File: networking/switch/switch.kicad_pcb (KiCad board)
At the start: 4 copper layers, 64.8 x 62.8 mm, 86 parts, among them J1 LDO IN, J3 3.3V IN, J4 PHY 5, J5 PHY 4, J6 PHY 3, J7 PHY 2, J8 PHY 1, SW1 AFT, SW2 F_PWR_OFF, T1 QT24A23-ALT, T2 QT24A23, U1 LM1117MP-3.3, U2 24LC01, U3 IP175G, U4 BT16A07, Y1 25MHz

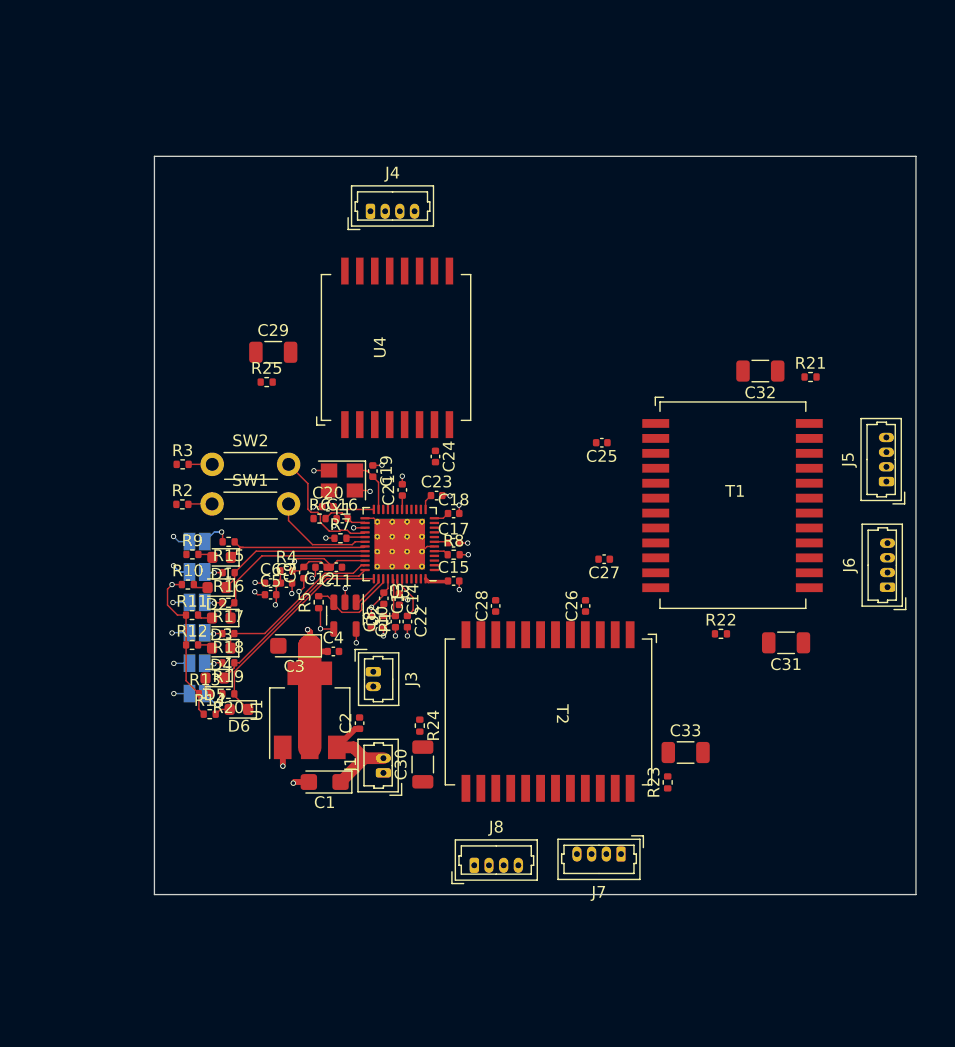
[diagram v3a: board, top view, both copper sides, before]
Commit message: Feat[switch]: Minor rerouting
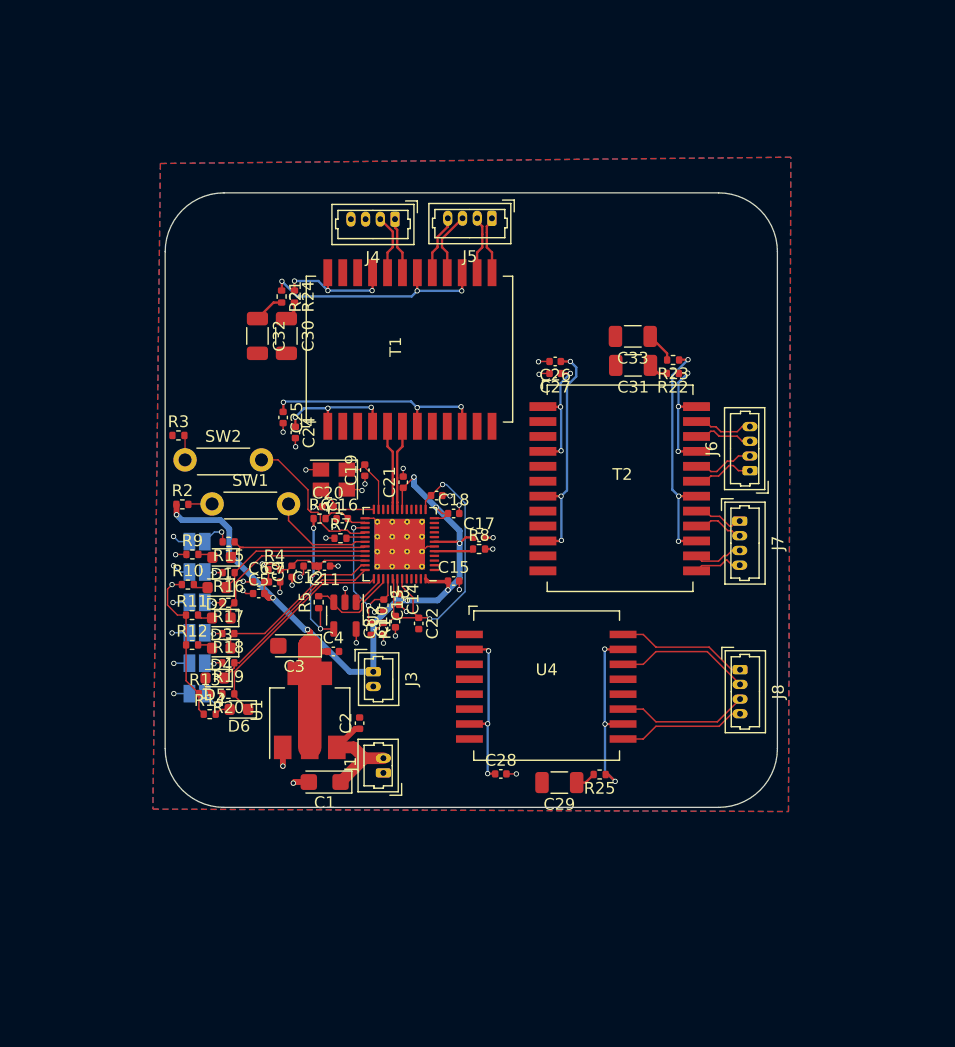
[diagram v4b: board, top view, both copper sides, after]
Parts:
- moved R21 45.5 mm to (114.9, 80.4), turned to -90 degrees
- moved C29 44.0 mm to (138.6, 121.7), turned to 180 degrees
- moved R25 43.8 mm to (142.0, 121.1), turned to 180 degrees
- moved C32 42.9 mm to (112.9, 83.8), turned to -90 degrees
- moved J5 40.3 mm to (132.8, 73.7), turned to 180 degrees
- moved C30 38.2 mm to (115.3, 83.8), turned to -90 degrees
- moved R24 38.0 mm to (116.0, 80.4)
- moved R23 35.9 mm to (148.2, 85.8), turned to 180 degrees
- moved C33 35.7 mm to (144.8, 83.8), turned to 180 degrees
- moved U4 31.4 mm to (137.4, 113.5), turned to 0 degrees
- moved T1 30.5 mm to (125.8, 84.9), turned to 90 degrees
- moved J7 30.1 mm to (153.9, 99.5), turned to -90 degrees
- moved J8 28.1 mm to (153.9, 112.1), turned to -90 degrees
- moved C25 27.2 mm to (115.1, 90.7), turned to -90 degrees
- moved C31 26.9 mm to (144.8, 86.3)
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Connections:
- C30 pad 1: /Magnetics/REF0 -> /Magnetics/REF4
- J8 pad 1: /Magnetics/RX0+ -> /Magnetics/TX0+
- J8 pad 2: /Magnetics/RX0- -> /Magnetics/TX0-
- J8 pad 3: /Magnetics/TX0+ -> /Magnetics/RX0+
- J8 pad 4: /Magnetics/TX0- -> /Magnetics/RX0-
- R24 pad 2: /Magnetics/REF0 -> /Magnetics/REF4
- R25 pad 1: /Magnetics/REF4 -> /Magnetics/REF0
- T1 pad 1: /Magnetics/CT3 -> /Magnetics/CT4
- T1 pad 10: /Magnetics/CT2 -> /Magnetics/CT3
- T1 pad 11: /IP175G/RXIM2 -> /IP175G/RXIM3
- T1 pad 12: /IP175G/RXIP2 -> /IP175G/RXIP3
- T1 pad 13: /Magnetics/RX2+ -> /Magnetics/RX3+
- T1 pad 14: /Magnetics/RX2- -> /Magnetics/RX3-
- T1 pad 15: Net-(R22-Pad1) -> Net-(R21-Pad1)
- T1 pad 16: /Magnetics/TX2+ -> /Magnetics/TX3+
- T1 pad 17: /Magnetics/TX2- -> /Magnetics/TX3-
- T1 pad 18: Net-(R22-Pad1) -> Net-(R21-Pad1)
- T1 pad 19: /Magnetics/RX3+ -> /Magnetics/RX4+
- T1 pad 2: /IP175G/TXOM3 -> /IP175G/RXIP4
- T1 pad 20: /Magnetics/RX3- -> /Magnetics/RX4-
- T1 pad 21: Net-(R21-Pad1) -> Net-(R24-Pad1)
- T1 pad 22: /Magnetics/TX3+ -> /Magnetics/TX4+
- T1 pad 23: /Magnetics/TX3- -> /Magnetics/TX4-
- T1 pad 24: Net-(R21-Pad1) -> Net-(R24-Pad1)
- T1 pad 3: /IP175G/TXOP3 -> /IP175G/RXIM4
- T1 pad 4: /Magnetics/CT3 -> /Magnetics/CT4
- T1 pad 5: /IP175G/RXIM3 -> /IP175G/TXO4+
- T1 pad 6: /IP175G/RXIP3 -> /IP175G/TXO4-
- T1 pad 7: /Magnetics/CT2 -> /Magnetics/CT3
- T1 pad 8: /IP175G/TXOM2 -> /IP175G/TXOM3
- T1 pad 9: /IP175G/TXOP2 -> /IP175G/TXOP3
- T2 pad 1: /Magnetics/CT1 -> /Magnetics/CT2
- T2 pad 10: /Magnetics/CT0 -> /Magnetics/CT1
- T2 pad 11: /IP175G/RXIM0 -> /IP175G/TXOP1
- T2 pad 12: /IP175G/RXIP0 -> /IP175G/TXOM1
- T2 pad 13: /Magnetics/RX0+ -> /Magnetics/TX1-
- T2 pad 14: /Magnetics/RX0- -> /Magnetics/TX1+
- T2 pad 15: Net-(R24-Pad1) -> Net-(R23-Pad1)
- T2 pad 16: /Magnetics/TX0+ -> /Magnetics/RX1-
- T2 pad 17: /Magnetics/TX0- -> /Magnetics/RX1+
- T2 pad 18: Net-(R24-Pad1) -> Net-(R23-Pad1)
- T2 pad 19: /Magnetics/TX1- -> /Magnetics/RX2+
- T2 pad 2: /IP175G/RXIP1 -> /IP175G/TXOM2
- T2 pad 20: /Magnetics/TX1+ -> /Magnetics/RX2-
- T2 pad 21: Net-(R23-Pad1) -> Net-(R22-Pad1)
- T2 pad 22: /Magnetics/RX1- -> /Magnetics/TX2+
- T2 pad 23: /Magnetics/RX1+ -> /Magnetics/TX2-
- T2 pad 24: Net-(R23-Pad1) -> Net-(R22-Pad1)
- T2 pad 3: /IP175G/RXIM1 -> /IP175G/TXOP2
- T2 pad 4: /Magnetics/CT1 -> /Magnetics/CT2
- T2 pad 5: /IP175G/TXOP1 -> /IP175G/RXIM2
- T2 pad 6: /IP175G/TXOM1 -> /IP175G/RXIP2
- T2 pad 7: /Magnetics/CT0 -> /Magnetics/CT1
- T2 pad 8: /IP175G/TXOM0 -> /IP175G/RXIP1
- T2 pad 9: /IP175G/TXOP0 -> /IP175G/RXIM1
- U3 pad 19: /IP175G/TXOM4 -> /IP175G/TXO4-
- U3 pad 20: /IP175G/TXOP4 -> /IP175G/TXO4+
- U4 pad 1: /IP175G/RXIP4 -> /IP175G/TXOM0
- U4 pad 10: /Magnetics/REF4 -> /Magnetics/REF0
- U4 pad 11: /Magnetics/TX4+ -> /Magnetics/RX0+
- U4 pad 14: /Magnetics/RX4- -> /Magnetics/TX0-
- U4 pad 15: /Magnetics/REF4 -> /Magnetics/REF0
- U4 pad 16: /Magnetics/RX4+ -> /Magnetics/TX0+
- U4 pad 2: /Magnetics/CT4 -> /Magnetics/CT0
- U4 pad 3: /IP175G/RXIM4 -> /IP175G/TXOP0
- U4 pad 6: /IP175G/TXOP4 -> /IP175G/RXIM0
- U4 pad 7: /Magnetics/CT4 -> /Magnetics/CT0
- U4 pad 8: /IP175G/TXOM4 -> /IP175G/RXIP0
- U4 pad 9: /Magnetics/TX4- -> /Magnetics/RX0-
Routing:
- net VCC: track 33.7 -> 77.2 mm, vias 3 -> 8
- net Net-(R23-Pad1): track 0.00 -> 20.1 mm, vias 0 -> 3
- net Net-(R21-Pad1): track 0.00 -> 19.9 mm, vias 0 -> 3
- net /Magnetics/CT1: track 0.00 -> 19.9 mm, vias 0 -> 3
- net /Magnetics/CT3: track 0.00 -> 19.5 mm, vias 0 -> 3
- net +1.1VA: track 11.4 -> 29.7 mm, vias 0 -> 2
- net /Magnetics/REF0: track 0.00 -> 15.8 mm, vias 0 -> 3
- net /Magnetics/CT0: track 0.00 -> 14.4 mm, vias 0 -> 3
- net /Magnetics/TX0-: track 0.00 -> 11.6 mm
- net /Magnetics/RX0+: track 0.00 -> 11.2 mm
- net /Magnetics/TX0+: track 0.00 -> 11.2 mm
- net Net-(R22-Pad1): track 0.00 -> 10.9 mm, vias 0 -> 3
- net /Magnetics/RX0-: track 0.00 -> 10.8 mm
- net /Magnetics/CT2: track 0.00 -> 10.8 mm, vias 0 -> 3
- net Net-(R24-Pad1): track 0.00 -> 10.8 mm, vias 0 -> 3
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- added copper zone on B.Cu, net GND
- added copper zone on F.Cu, net GND
- added copper zone on In1.Cu, net GND
- added copper zone on In2.Cu, net GND
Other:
- board size 64.8 x 62.8 mm -> 52.1 x 52.3 mm
- board text removed: "@TODO: change magnetics so that single transformer is on 0, the other two dual transformers handle 1,2,3,4"

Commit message: Feat[switch]: Routed magnetics
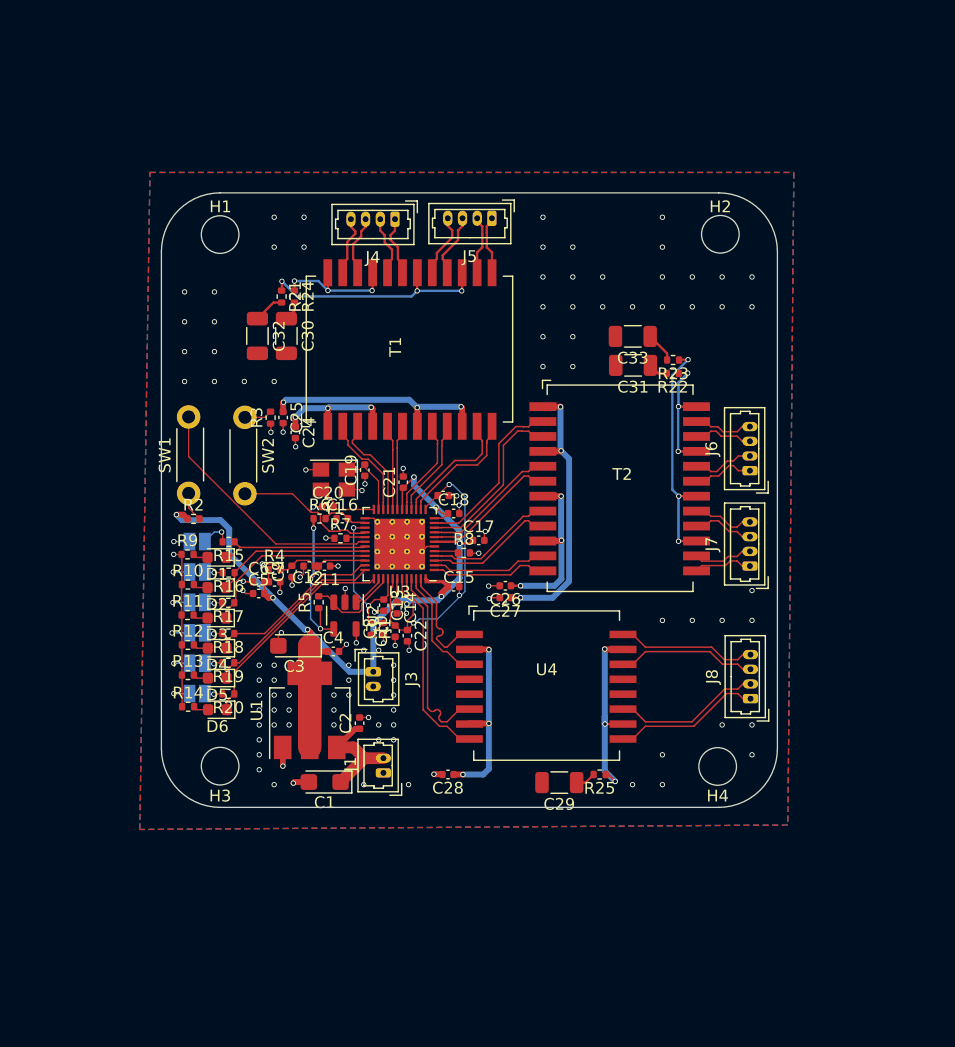
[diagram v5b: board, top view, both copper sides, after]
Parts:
- added H1: MountingHole, MountingHole:MountingHole_3.2mm_M3, F.Cu at (109.7, 75.1)
- added H2: MountingHole, MountingHole:MountingHole_3.2mm_M3, F.Cu at (152.2, 75.1)
- added H3: MountingHole, MountingHole:MountingHole_3.2mm_M3, F.Cu at (109.7, 120.3)
- added H4: MountingHole, MountingHole:MountingHole_3.2mm_M3, F.Cu at (152.0, 120.4)
- moved C26 19.5 mm to (134.0, 105.0)
- moved C27 19.5 mm to (134.0, 106.0)
- moved R3 7.98 mm to (114.0, 90.7), turned to 90 degrees
- moved SW2 6.25 mm to (111.8, 90.7), turned to -90 degrees
- moved C28 4.49 mm to (129.1, 121.1), turned to 180 degrees
- moved J7 3.92 mm to (154.8, 103.3), turned to 90 degrees
- moved J8 2.62 mm to (154.8, 114.6), turned to 90 degrees
- moved SW1 2.19 mm to (107.0, 97.1), turned to 90 degrees
- moved R13 2.14 mm to (107.0, 112.6)
- moved R14 1.94 mm to (107.0, 115.3)
- moved D6 1.83 mm to (109.5, 115.5)
- moved R2 1.56 mm to (107.4, 99.3)
- moved C22 1.42 mm to (125.6, 109.2)
- moved R8 1.33 mm to (130.4, 102.2)
- moved C10 0.81 mm to (124.6, 108.9)
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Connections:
- net /IP175G/RXIM0 renamed /IP175G/RXI0-
- net /IP175G/RXIM1 renamed /IP175G/RXI1-
- net /IP175G/RXIM2 renamed /IP175G/RXI2-
- net /IP175G/RXIM3 renamed /IP175G/RXI3-
- net /IP175G/RXIM4 renamed /IP175G/RXI4-
- net /IP175G/RXIP0 renamed /IP175G/RXI0+
- net /IP175G/RXIP1 renamed /IP175G/RXI1+
- net /IP175G/RXIP2 renamed /IP175G/RXI2+
- net /IP175G/RXIP3 renamed /IP175G/RXI3+
- net /IP175G/RXIP4 renamed /IP175G/RXI4+
- net /IP175G/TXOM0 renamed /IP175G/TXO0-
- net /IP175G/TXOM1 renamed /IP175G/TXO1-
- net /IP175G/TXOM2 renamed /IP175G/TXO2-
- net /IP175G/TXOM3 renamed /IP175G/TXO3-
- net /IP175G/TXOP0 renamed /IP175G/TXO0+
- net /IP175G/TXOP1 renamed /IP175G/TXO1+
- net /IP175G/TXOP2 renamed /IP175G/TXO2+
- net /IP175G/TXOP3 renamed /IP175G/TXO3+
- J7 pad 1: /Magnetics/RX1+ -> /Magnetics/TX1-
- J7 pad 2: /Magnetics/RX1- -> /Magnetics/TX1+
- J7 pad 3: /Magnetics/TX1+ -> /Magnetics/RX1-
- J7 pad 4: /Magnetics/TX1- -> /Magnetics/RX1+
- J8 pad 1: /Magnetics/TX0+ -> /Magnetics/RX0-
- J8 pad 2: /Magnetics/TX0- -> /Magnetics/RX0+
- J8 pad 3: /Magnetics/RX0+ -> /Magnetics/TX0-
- J8 pad 4: /Magnetics/RX0- -> /Magnetics/TX0+
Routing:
- net /IP175G/RXI0+: track 0.00 -> 16.7 mm
- net /IP175G/RXI0-: track 0.00 -> 16.6 mm
- net /IP175G/TXO2-: track 0.00 -> 14.8 mm
- net /IP175G/TXO2+: track 0.00 -> 14.8 mm
- net /Magnetics/CT2: track 10.8 -> 23.7 mm
- net /IP175G/AFT: track 8.87 -> 21.5 mm
- net /IP175G/RXI2-: track 0.00 -> 11.6 mm
- net /IP175G/RXI2+: track 0.00 -> 11.6 mm
- net /IP175G/RXI1+: track 0.00 -> 11.0 mm
- net /IP175G/RXI1-: track 0.00 -> 11.0 mm
- net /IP175G/RXI3+: track 0.00 -> 10.6 mm
- net /IP175G/RXI3-: track 0.00 -> 10.6 mm
- net /IP175G/TXO1-: track 0.00 -> 9.92 mm
- net /IP175G/TXO1+: track 0.00 -> 9.92 mm
- net /IP175G/TXO0+: track 0.00 -> 9.84 mm
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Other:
- board size 52.1 x 52.3 mm -> 52.4 x 52.3 mm
- board text removed: "@TODO: complete layout"
- board text removed: "@TODO: optimize termination scheme"
- board text removed: "@TODO: redesign magnetics to minimize routing and maximize signal integrity and pinout"

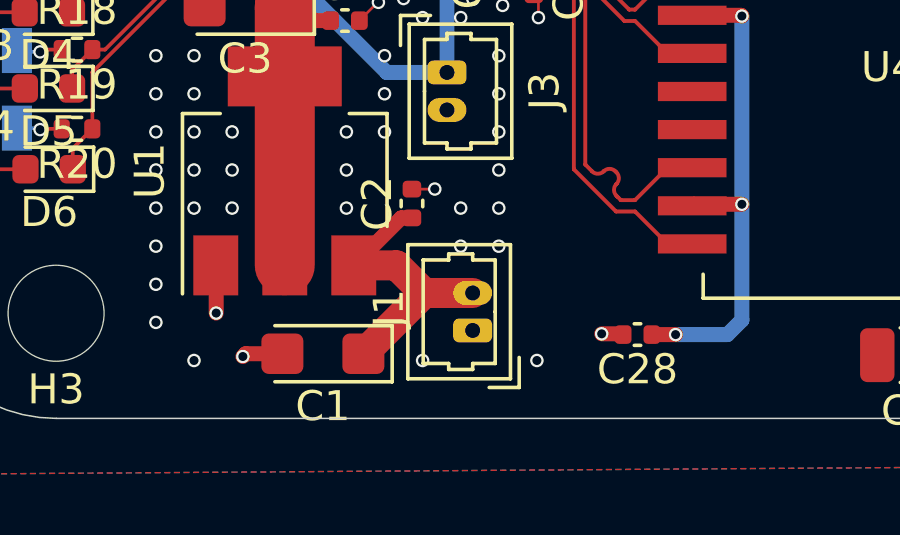
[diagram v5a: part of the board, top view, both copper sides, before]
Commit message: Feat[switch]: rotated J1
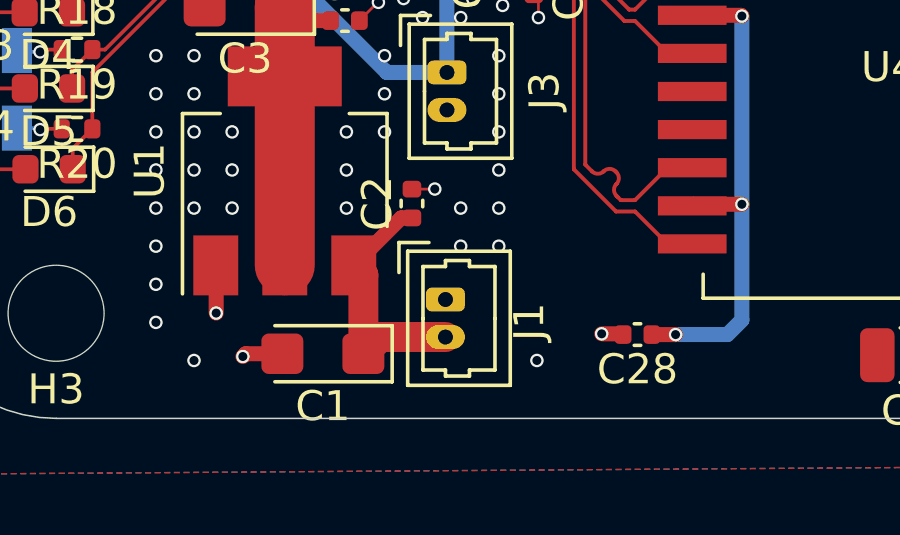
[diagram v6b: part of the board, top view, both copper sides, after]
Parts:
- moved J1 1.37 mm to (122.7, 119.9), turned to -90 degrees
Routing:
- net Net-(J1-Pin_2): track 9.80 -> 8.64 mm
- net GND: vias 126 -> 125

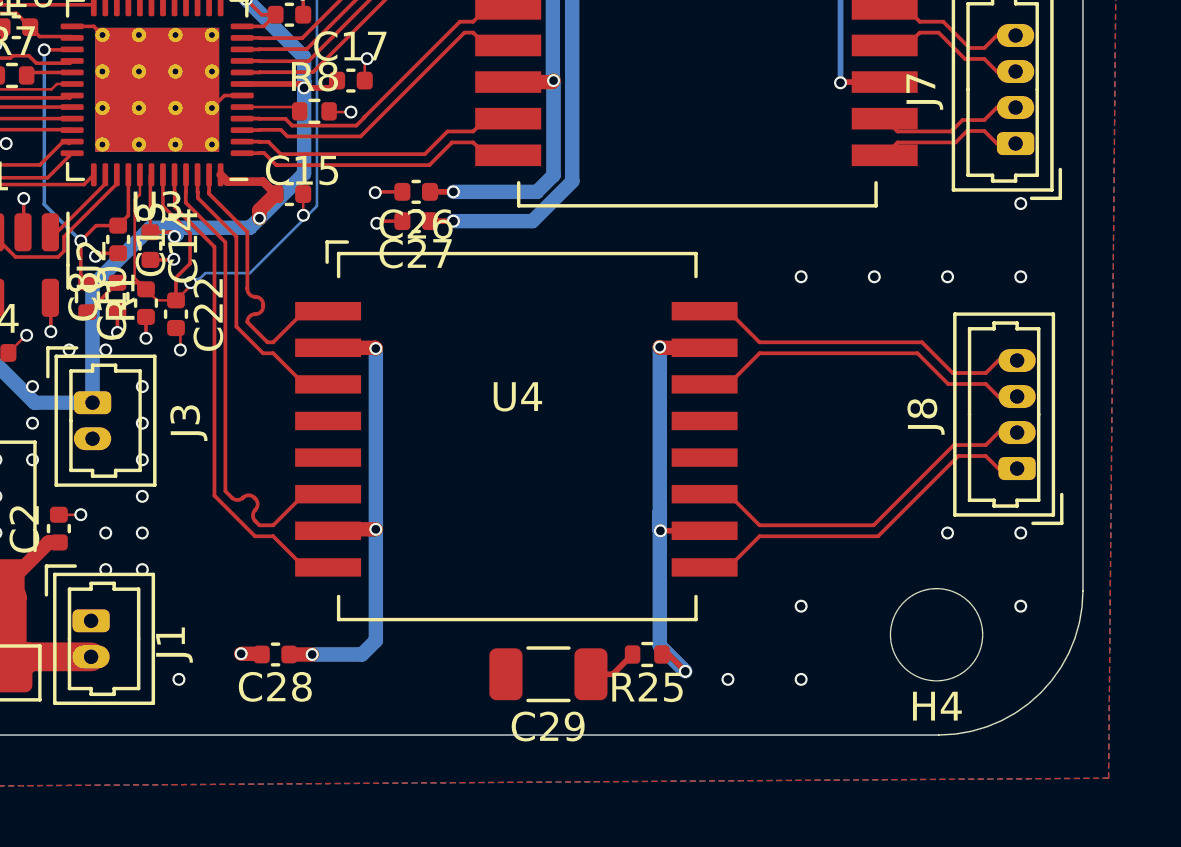
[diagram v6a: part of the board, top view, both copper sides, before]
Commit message: Feat[switch]: Fixed single transformer footprint, added 3d models
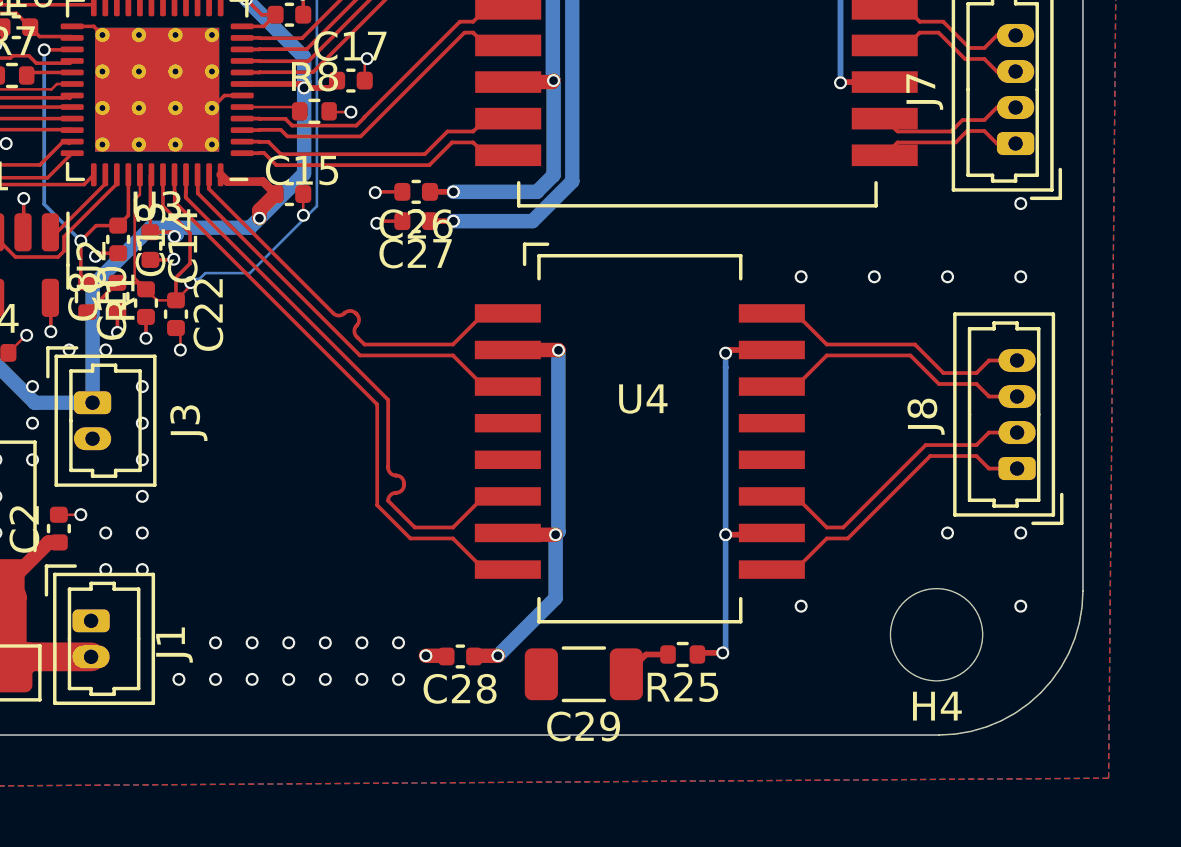
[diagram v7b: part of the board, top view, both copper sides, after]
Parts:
- moved C28 6.41 mm to (135.5, 121.1)
- moved U4 4.35 mm to (141.7, 113.6)
- moved C29 1.23 mm to (139.8, 121.7)
- moved R25 1.23 mm to (143.2, 121.1)
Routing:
- net /IP175G/TXO0+: track 9.84 -> 14.2 mm
- net /IP175G/TXO0-: track 9.80 -> 14.1 mm
- net /IP175G/RXI0-: track 16.6 -> 19.8 mm
- net /IP175G/RXI0+: track 16.7 -> 19.8 mm
- net /Magnetics/TX0+: track 11.9 -> 9.55 mm
- net /Magnetics/TX0-: track 11.9 -> 9.55 mm
- net /Magnetics/RX0+: track 12.6 -> 10.3 mm
- net /Magnetics/RX0-: track 12.6 -> 10.3 mm
- net /Magnetics/REF0: track 16.4 -> 14.6 mm
- net /Magnetics/CT0: track 16.7 -> 15.7 mm
- net GND: track 42.9 -> 42.8 mm, vias 125 -> 135
